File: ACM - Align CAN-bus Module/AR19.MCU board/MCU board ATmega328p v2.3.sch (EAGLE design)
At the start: 40 parts, among them IC1 ATMEGA328P-MMH, IC2 MIC5239-5.0YS_TR, IC3 MCP25625-E_ML, J1 AVR_SPI_PROG_3X2NS

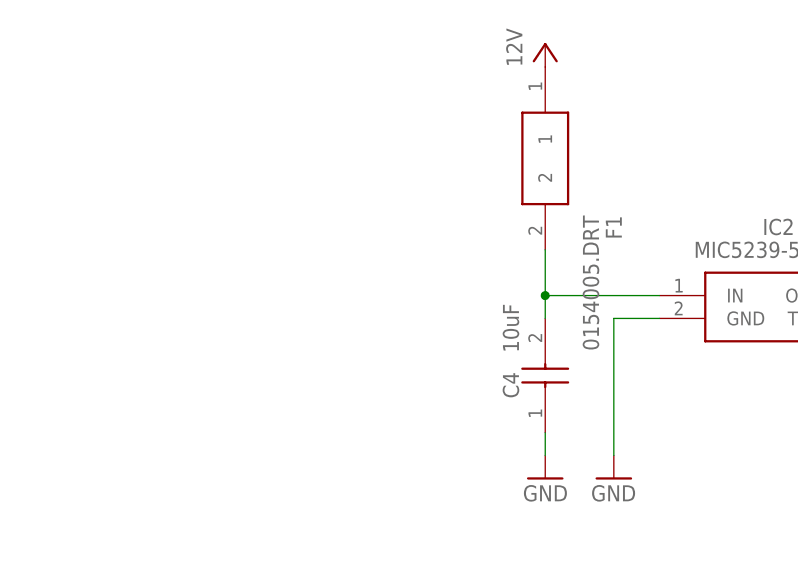
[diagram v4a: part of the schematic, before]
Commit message: Added: Orange Power LED with 500ohm resistor
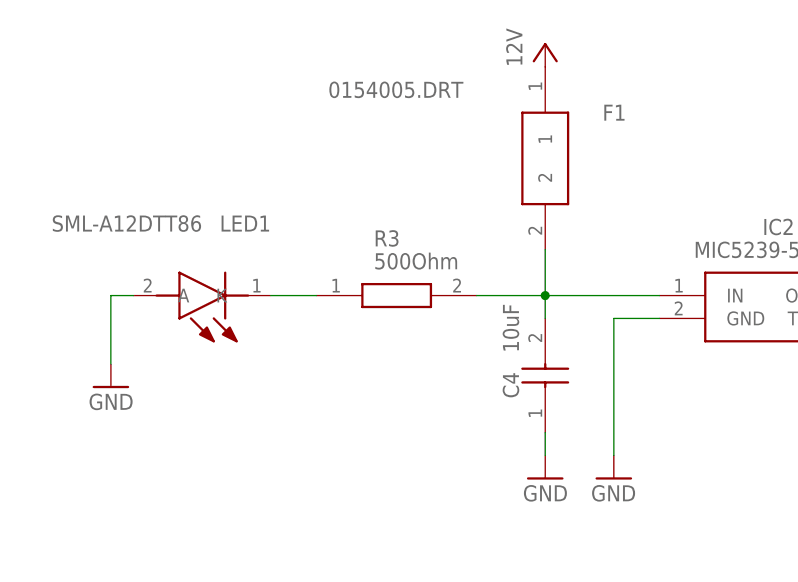
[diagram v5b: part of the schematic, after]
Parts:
- added LED1: SML-A12DTT86, SML-A12DTT86:SML-A12DTT86
- added R3: 500Ohm, CRCW040295R3FKED(0402):CRCW040295R3FKED
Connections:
- new net N$3: LED1.K, R3.1
- net GND: now also LED1.A
- net N$2: now also R3.2
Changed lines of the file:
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@@
 <part name="U$2" library="FA-20H 16.0000MF20X-B" deviceset="FA-20H" device=""/>
 <part name="F1" library="0154005(Fuseholder)DRT" deviceset="0154005.DRT" device=""/>
+<part name="LED1" library="SML-A12DTT86" deviceset="SML-A12DTT86" device=""/>
+<part name="GND1" library="supply1" library_urn="urn:adsk.eagle:library:371" deviceset="GND" device=""/>
+<part name="R3" library="CRCW040295R3FKED(0402)" deviceset="CRCW040295R3FKED" device="" value="500Ohm"/>
 </parts>
 <sheets>
@@
 <instance part="U$2" gate="G$1" x="335.28" y="99.06" smashed="yes"/>
 <instance part="F1" gate="G$1" x="-30.48" y="187.96" smashed="yes" rot="R270">
-<attribute name="NAME" x="-22.86" y="171.45" size="1.778" layer="95" rot="R270" align="center-left"/>
-<attribute name="VALUE" x="-25.4" y="171.45" size="1.778" layer="96" rot="R270" align="center-left"/>
+<attribute name="NAME" x="-24.13" y="182.88" size="1.778" layer="95" align="center-left"/>
+<attribute name="VALUE" x="-54.61" y="185.42" size="1.778" layer="96" align="center-left"/>
+</instance>
+<instance part="LED1" gate="G$1" x="-60.96" y="162.56" smashed="yes" rot="R180">
+<attribute name="NAME" x="-60.96" y="171.45" size="1.778" layer="95" rot="R180"/>
+<attribute name="VALUE" x="-68.58" y="171.45" size="1.778" layer="96" rot="R180"/>
+</instance>
+<instance part="GND1" gate="1" x="-78.74" y="152.4" smashed="yes" rot="MR0">
+<attribute name="VALUE" x="-76.2" y="149.86" size="1.778" layer="96" rot="MR0"/>
+</instance>
+<instance part="R3" gate="G$1" x="-55.88" y="162.56" smashed="yes">
+<attribute name="NAME" x="-49.53" y="168.91" size="1.778" layer="95" align="center-left"/>
+<attribute name="VALUE" x="-49.53" y="166.37" size="1.778" layer="96" align="center-left"/>
 </instance>
 </instances>
@@
 <wire x1="350.52" y1="45.72" x2="350.52" y2="43.18" width="0.1524" layer="91"/>
 </segment>
+<segment>
+<pinref part="LED1" gate="G$1" pin="A"/>
+<wire x1="-76.2" y1="162.56" x2="-78.74" y2="162.56" width="0.1524" layer="91"/>
+<wire x1="-78.74" y1="162.56" x2="-78.74" y2="154.94" width="0.1524" layer="91"/>
+<pinref part="GND1" gate="1" pin="GND"/>
+</segment>
 </net>
 <net name="MOSI" class="0">
@@
 <wire x1="-17.78" y1="162.56" x2="-30.48" y2="162.56" width="0.1524" layer="91"/>
 <junction x="-30.48" y="162.56"/>
-</segment>
-</net>
+<pinref part="R3" gate="G$1" pin="2"/>
+<wire x1="-38.1" y1="162.56" x2="-30.48" y2="162.56" width="0.1524" layer="91"/>
+</segment>
+</net>
+<net name="N$3" class="0">
+<segment>
+<pinref part="LED1" gate="G$1" pin="K"/>
+<pinref part="R3" gate="G$1" pin="1"/>
+<wire x1="-60.96" y1="162.56" x2="-55.88" y2="162.56" width="0.1524" layer="91"/>
+</segment>
+</net>

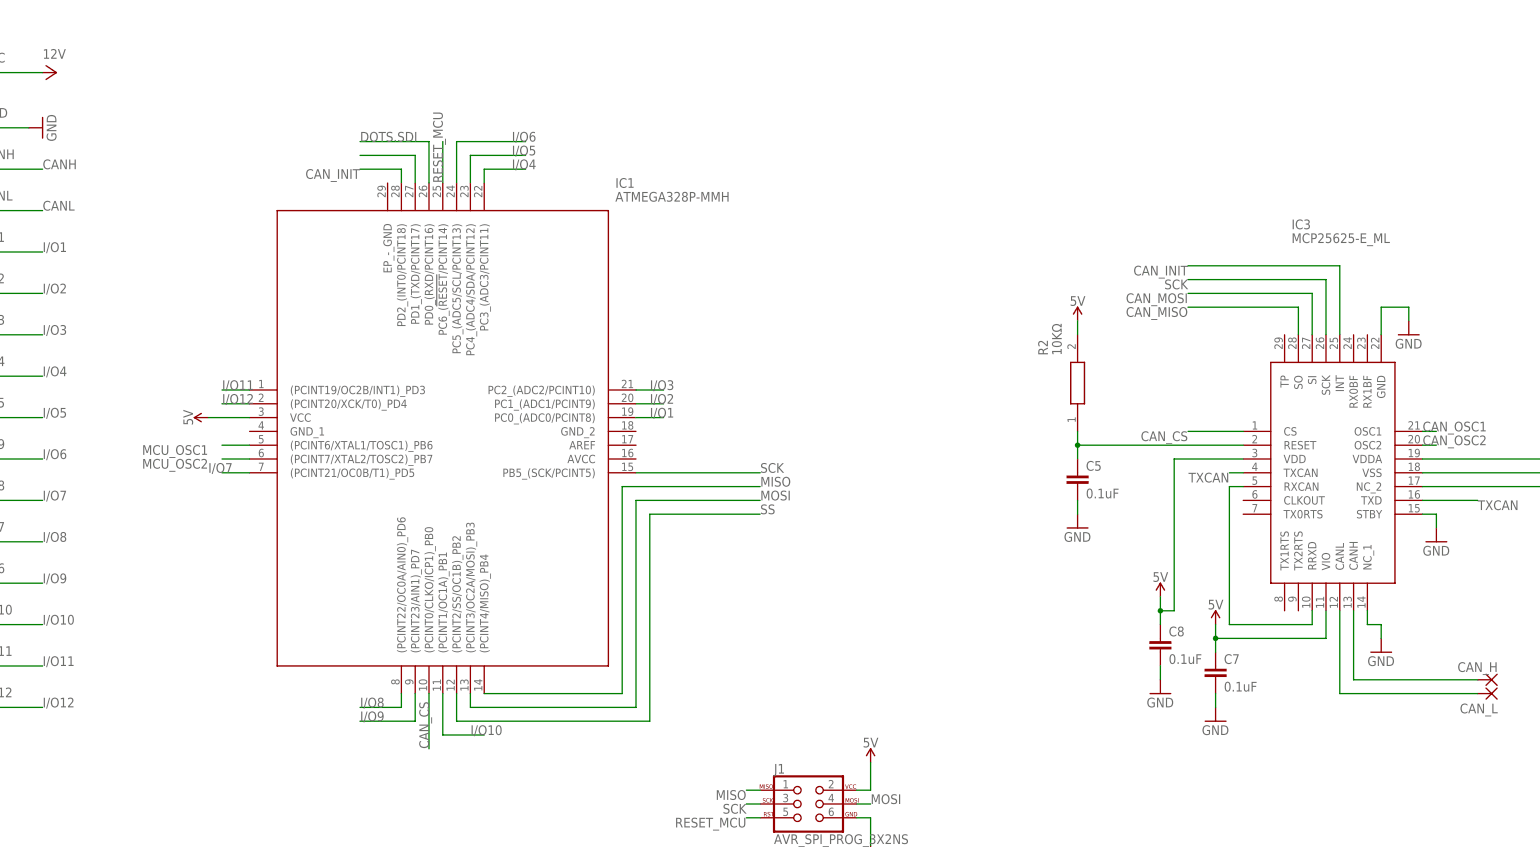
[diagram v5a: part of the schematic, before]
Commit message: Added: Datasheets and capacitors to ATMEGA328p
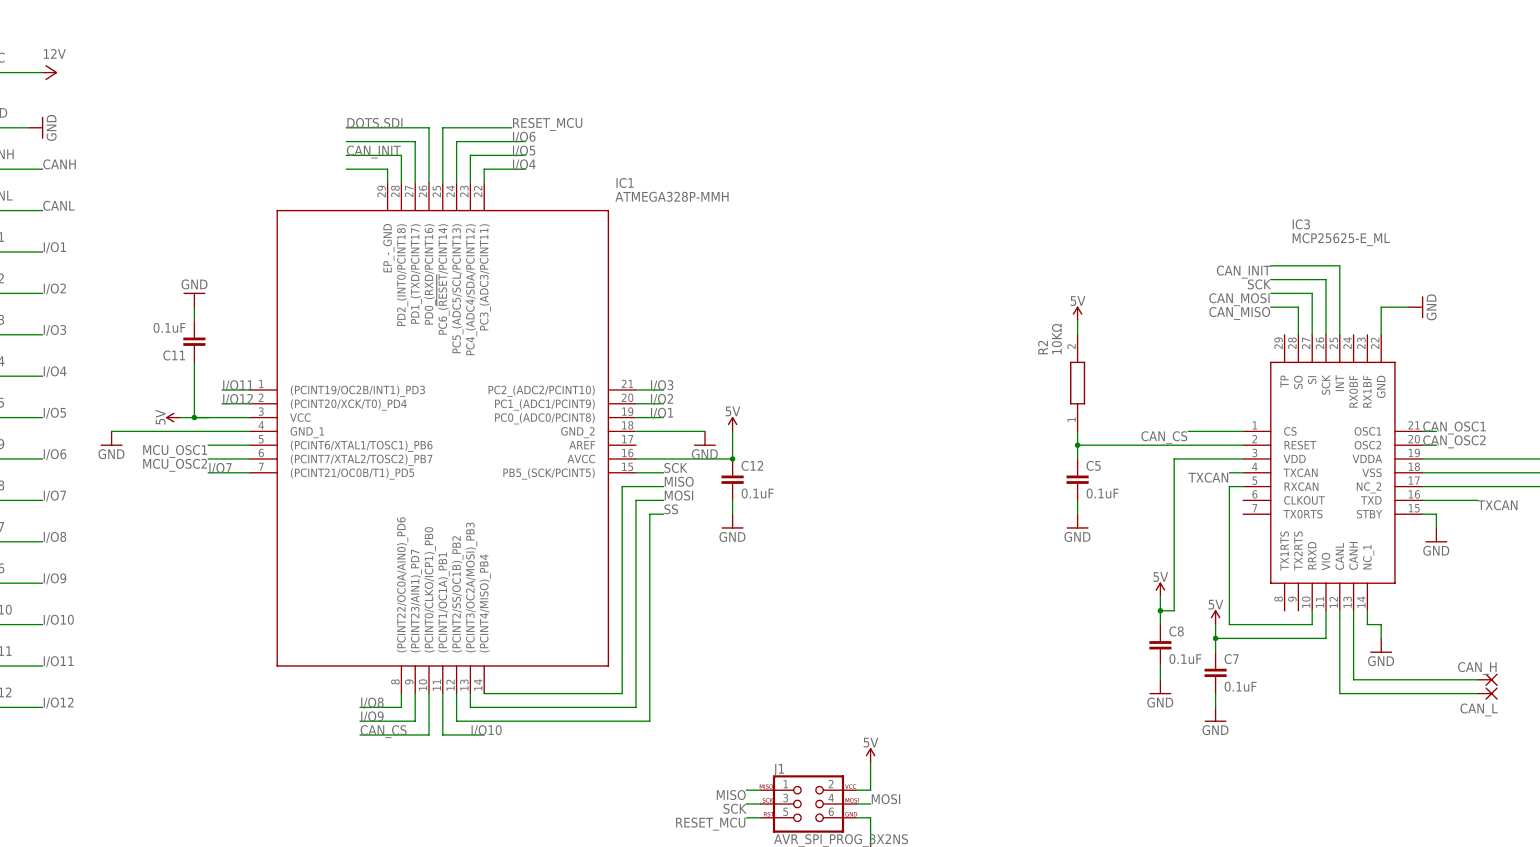
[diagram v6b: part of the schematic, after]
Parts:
- added C11, C12: 0.1uF, eagle-ltspice:CC0603
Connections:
- new net N$4: IC1.EP_-_GND
- net 5V: now also C11.1, C12.1, IC1.AVCC
- net GND: now also C11.2, C12.2, IC1.GND_1, IC1.GND_2

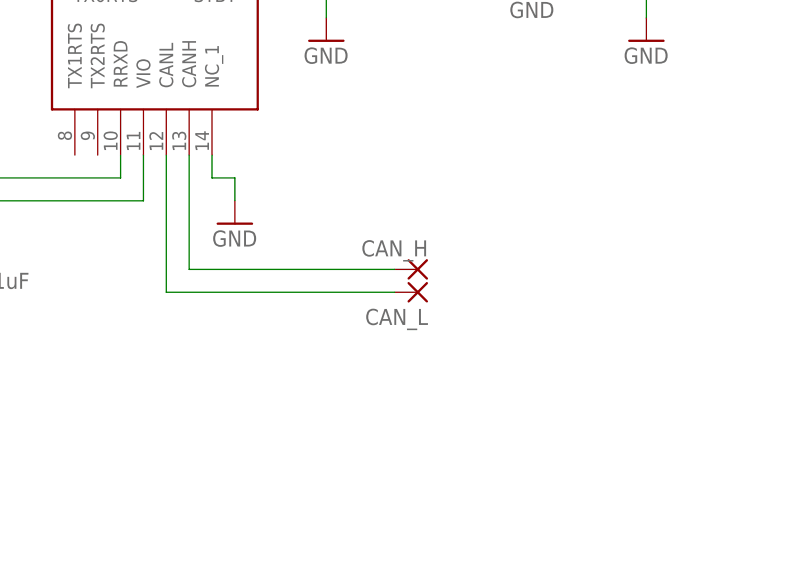
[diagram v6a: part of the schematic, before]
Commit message: Removed: Extra CAN port and Tested Board routing
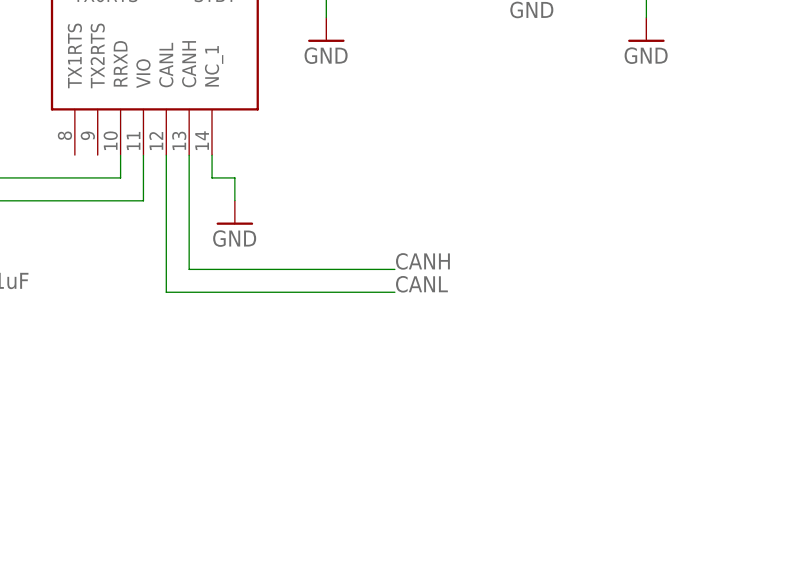
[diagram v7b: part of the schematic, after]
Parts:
- removed CAN_H, CAN_L: (no value), wirepad:2,15/1,0
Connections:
- net CANH: no longer CAN_H.P
- net CANL: no longer CAN_L.P
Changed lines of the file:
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@@
 <part name="GND5" library="supply1" library_urn="urn:adsk.eagle:library:371" deviceset="GND" device=""/>
 <part name="GND6" library="supply1" library_urn="urn:adsk.eagle:library:371" deviceset="GND" device=""/>
-<part name="CAN_H" library="wirepad" library_urn="urn:adsk.eagle:library:412" deviceset="2,15/1,0" device="" package3d_urn="urn:adsk.eagle:package:30831/1"/>
-<part name="CAN_L" library="wirepad" library_urn="urn:adsk.eagle:library:412" deviceset="2,15/1,0" device="" package3d_urn="urn:adsk.eagle:package:30831/1"/>
 <part name="C5" library="eagle-ltspice" library_urn="urn:adsk.eagle:library:217" deviceset="C" device="C0603" package3d_urn="urn:adsk.eagle:package:13262/1" value="0.1uF"/>
 <part name="R2" library="CPF0201D10KC1" deviceset="CPF0201D10KC1" device="" value="10KΩ"/>
@@
 <attribute name="VALUE" x="-27.94" y="139.7" size="1.778" layer="96" rot="MR0"/>
 </instance>
-<instance part="CAN_H" gate="1" x="238.76" y="5.08" smashed="yes" rot="R180">
-<attribute name="NAME" x="239.903" y="8.3058" size="1.778" layer="95" rot="R180"/>
-<attribute name="VALUE" x="239.903" y="8.382" size="1.778" layer="96" rot="R180"/>
-</instance>
-<instance part="CAN_L" gate="1" x="238.76" y="2.54" smashed="yes" rot="R180">
-<attribute name="NAME" x="239.903" y="0.6858" size="1.778" layer="95" rot="R180"/>
-<attribute name="VALUE" x="239.903" y="5.842" size="1.778" layer="96" rot="R180"/>
-</instance>
 <instance part="C5" gate="G$1" x="162.56" y="43.18" smashed="yes">
 <attribute name="NAME" x="164.084" y="43.561" size="1.778" layer="95"/>
@@
 <wire x1="210.82" y1="17.78" x2="210.82" y2="2.54" width="0.1524" layer="91"/>
 <wire x1="210.82" y1="2.54" x2="236.22" y2="2.54" width="0.1524" layer="91"/>
-<pinref part="CAN_L" gate="1" pin="P"/>
+<label x="236.22" y="2.54" size="1.778" layer="95"/>
 </segment>
 </net>
@@
 <wire x1="213.36" y1="17.78" x2="213.36" y2="5.08" width="0.1524" layer="91"/>
 <wire x1="236.22" y1="5.08" x2="213.36" y2="5.08" width="0.1524" layer="91"/>
-<pinref part="CAN_H" gate="1" pin="P"/>
-</segment>
-</net>
+<label x="236.22" y="5.08" size="1.778" layer="95"/>
+</segment>
+</net>
